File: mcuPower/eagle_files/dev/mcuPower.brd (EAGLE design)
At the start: 27 x 45.1 mm, 8 parts, among them P1 CR2032, P2 CR2032, U1 PQ070XF01SZH

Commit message: most complete to date files
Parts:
- moved P1 0.45 mm to (12.8, 32.5)
- moved P2 0.45 mm to (12.8, 32.5)
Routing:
- net GND: track 52.1 -> 50.4 mm
- net VCC: track 37.8 -> 38.6 mm
- net N$1: track 10.5 -> 11.0 mm
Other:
- board text added: "F. Lee mcuPower 8/25/13"
- board text removed: "F. Lee mcuPower 8/17/13"
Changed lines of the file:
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@@
 <layer number="27" name="tValues" color="7" fill="1" visible="yes" active="yes"/>
 <layer number="28" name="bValues" color="7" fill="1" visible="yes" active="yes"/>
-<layer number="29" name="tStop" color="7" fill="3" visible="yes" active="yes"/>
-<layer number="30" name="bStop" color="7" fill="6" visible="yes" active="yes"/>
-<layer number="31" name="tCream" color="7" fill="4" visible="yes" active="yes"/>
-<layer number="32" name="bCream" color="7" fill="5" visible="yes" active="yes"/>
+<layer number="29" name="tStop" color="7" fill="3" visible="no" active="yes"/>
+<layer number="30" name="bStop" color="7" fill="6" visible="no" active="yes"/>
+<layer number="31" name="tCream" color="7" fill="4" visible="no" active="yes"/>
+<layer number="32" name="bCream" color="7" fill="5" visible="no" active="yes"/>
 <layer number="33" name="tFinish" color="6" fill="3" visible="no" active="yes"/>
 <layer number="34" name="bFinish" color="6" fill="6" visible="no" active="yes"/>
@@
 <layer number="109" name="fp9" color="7" fill="1" visible="no" active="yes"/>
 <layer number="110" name="fp0" color="7" fill="1" visible="no" active="yes"/>
-<layer number="111" name="LPC17xx" color="7" fill="1" visible="yes" active="yes"/>
-<layer number="112" name="tSilk" color="7" fill="1" visible="yes" active="yes"/>
+<layer number="111" name="LPC17xx" color="7" fill="1" visible="no" active="yes"/>
+<layer number="112" name="tSilk" color="7" fill="1" visible="no" active="yes"/>
 <layer number="116" name="Patch_BOT" color="9" fill="4" visible="yes" active="yes"/>
-<layer number="121" name="_tsilk" color="7" fill="1" visible="yes" active="yes"/>
-<layer number="122" name="_bsilk" color="7" fill="1" visible="yes" active="yes"/>
-<layer number="123" name="tTestmark" color="7" fill="1" visible="yes" active="yes"/>
-<layer number="124" name="bTestmark" color="7" fill="1" visible="yes" active="yes"/>
-<layer number="125" name="_tNames" color="7" fill="1" visible="yes" active="yes"/>
-<layer number="126" name="_bNames" color="7" fill="1" visible="yes" active="yes"/>
-<layer number="127" name="_tValues" color="7" fill="1" visible="yes" active="yes"/>
-<layer number="128" name="_bValues" color="7" fill="1" visible="yes" active="yes"/>
-<layer number="131" name="tAdjust" color="7" fill="1" visible="yes" active="yes"/>
+<layer number="121" name="_tsilk" color="7" fill="1" visible="no" active="yes"/>
+<layer number="122" name="_bsilk" color="7" fill="1" visible="no" active="yes"/>
+<layer number="123" name="tTestmark" color="7" fill="1" visible="no" active="yes"/>
+<layer number="124" name="bTestmark" color="7" fill="1" visible="no" active="yes"/>
+<layer number="125" name="_tNames" color="7" fill="1" visible="no" active="yes"/>
+<layer number="126" name="_bNames" color="7" fill="1" visible="no" active="yes"/>
+<layer number="127" name="_tValues" color="7" fill="1" visible="no" active="yes"/>
+<layer number="128" name="_bValues" color="7" fill="1" visible="no" active="yes"/>
+<layer number="131" name="tAdjust" color="7" fill="1" visible="no" active="yes"/>
 <layer number="132" name="bAdjust" color="7" fill="1" visible="no" active="yes"/>
 <layer number="144" name="Drill_legend" color="7" fill="1" visible="yes" active="yes"/>
 <layer number="150" name="Notes" color="7" fill="1" visible="no" active="yes"/>
 <layer number="151" name="HeatSink" color="7" fill="1" visible="yes" active="yes"/>
-<layer number="152" name="_bDocu" color="7" fill="1" visible="yes" active="yes"/>
+<layer number="152" name="_bDocu" color="7" fill="1" visible="no" active="yes"/>
 <layer number="153" name="FabDoc1" color="6" fill="1" visible="no" active="no"/>
 <layer number="154" name="FabDoc2" color="2" fill="1" visible="no" active="no"/>
@@
 <wire x1="27.02" y1="45.09" x2="0.03" y2="45.05" width="0" layer="20"/>
 <wire x1="0.03" y1="45.05" x2="0" y2="0" width="0" layer="20"/>
-<text x="25" y="20.2" size="1.016" layer="16" rot="MR0">F. Lee
+<text x="25.3" y="20.5" size="1.016" layer="22" rot="MR0">F. Lee
 mcuPower
-8/17/13</text>
+8/25/13</text>
 </plain>
 <attributes>
@@
 <attribute name="NAME" x="3.78" y="21.08" size="1.27" layer="25" rot="R180"/>
 </element>
-<element name="P1" library="freddyLibr" package="CR2032/2025" value="CR2032" x="13" y="32.1" smashed="yes" rot="R90">
-<attribute name="NAME" x="4.71" y="26.44" size="1.27" layer="25" rot="R180"/>
-</element>
-<element name="P2" library="freddyLibr" package="CR2032/2025" value="CR2032" x="13" y="32.1" smashed="yes" rot="MR0">
-<attribute name="NAME" x="25.41" y="37.46" size="1.27" layer="26" rot="MR0"/>
+<element name="P1" library="freddyLibr" package="CR2032/2025" value="CR2032" x="12.8" y="32.5" smashed="yes" rot="R90">
+<attribute name="NAME" x="6.01" y="23.54" size="1.27" layer="25" rot="R180"/>
+</element>
+<element name="P2" library="freddyLibr" package="CR2032/2025" value="CR2032" x="12.8" y="32.5" smashed="yes" rot="MR0">
+<attribute name="NAME" x="21.01" y="41.16" size="1.27" layer="26" rot="MR0"/>
 </element>
 </elements>
@@
 <contactref element="C1" pad="1"/>
 <contactref element="U1" pad="VIN"/>
-<contactref element="P2" pad="VCC_2"/>
 <wire x1="22.4" y1="10.39" x2="11.82" y2="10.39" width="0.4064" layer="16"/>
 <wire x1="11.82" y1="10.39" x2="8.43" y2="7" width="0.4064" layer="16"/>
-<wire x1="23.4" y1="30.5" x2="23.4" y2="21.1" width="0.4064" layer="1"/>
-<wire x1="23.4" y1="21.1" x2="25.7" y2="18.8" width="0.4064" layer="1"/>
-<wire x1="25.7" y1="18.8" x2="25.7" y2="13.69" width="0.4064" layer="1"/>
-<wire x1="25.7" y1="13.69" x2="22.4" y2="10.39" width="0.4064" layer="1"/>
+<contactref element="P2" pad="VCC_2"/>
+<wire x1="23.2" y1="30.9" x2="23.2" y2="21" width="0.4064" layer="1"/>
+<wire x1="23.2" y1="21" x2="25.4" y2="18.8" width="0.4064" layer="1"/>
+<wire x1="25.4" y1="18.8" x2="25.4" y2="12.5" width="0.4064" layer="1"/>
+<wire x1="25.4" y1="12.5" x2="23.3" y2="10.4" width="0.4064" layer="1"/>
+<wire x1="23.3" y1="10.4" x2="22.41" y2="10.4" width="0.4064" layer="1"/>
+<wire x1="22.41" y1="10.4" x2="22.4" y2="10.39" width="0.4064" layer="1"/>
 </signal>
 <signal name="GND">
@@
 <contactref element="JP1" pad="1"/>
 <contactref element="U1" pad="GND"/>
-<contactref element="P1" pad="GND"/>
-<wire x1="13" y1="32.1" x2="13" y2="31.3" width="0.4064" layer="1"/>
-<wire x1="13" y1="31.3" x2="4.7" y2="23" width="0.4064" layer="1"/>
-<via x="4.7" y="23" extent="1-16" drill="0.6"/>
-<wire x1="4.7" y1="23" x2="4.74" y2="23" width="0.4064" layer="16"/>
-<wire x1="4.74" y1="23" x2="10.8" y2="16.94" width="0.4064" layer="16"/>
 <wire x1="10.8" y1="16.94" x2="10.8" y2="13.7" width="0.4064" layer="16"/>
 <wire x1="10.8" y1="13.7" x2="10.8" y2="12.28" width="0.4064" layer="16"/>
@@
 <wire x1="22.4" y1="15.47" x2="12.57" y2="15.47" width="0.4064" layer="16"/>
 <wire x1="12.57" y1="15.47" x2="10.8" y2="13.7" width="0.4064" layer="16"/>
+<contactref element="P1" pad="GND"/>
+<wire x1="10.8" y1="16.94" x2="10.8" y2="17" width="0.4064" layer="16"/>
+<wire x1="10.8" y1="17" x2="7.1" y2="20.7" width="0.4064" layer="16"/>
+<via x="7.1" y="20.7" extent="1-16" drill="0.6"/>
+<wire x1="7.1" y1="20.7" x2="7.1" y2="26.8" width="0.4064" layer="1"/>
+<wire x1="7.1" y1="26.8" x2="12.8" y2="32.5" width="0.4064" layer="1"/>
 </signal>
 <signal name="N$2">
@@
 <contactref element="JP1" pad="4"/>
 </signal>
+<signal name="N$3">
+</signal>
 <signal name="N$1">
 <contactref element="P1" pad="VCC_1"/>
 <contactref element="P2" pad="GND"/>
-<wire x1="11.5" y1="21.7" x2="12.8" y2="30.6" width="0.4064" layer="16"/>
-<wire x1="12.8" y1="30.6" x2="13" y2="32.1" width="0.4064" layer="16"/>
-</signal>
-<signal name="N$3">
+<wire x1="11.3" y1="22.1" x2="11.3" y2="31" width="0.4064" layer="16"/>
+<wire x1="11.3" y1="31" x2="12.8" y2="32.5" width="0.4064" layer="16"/>
 </signal>
 </signals>

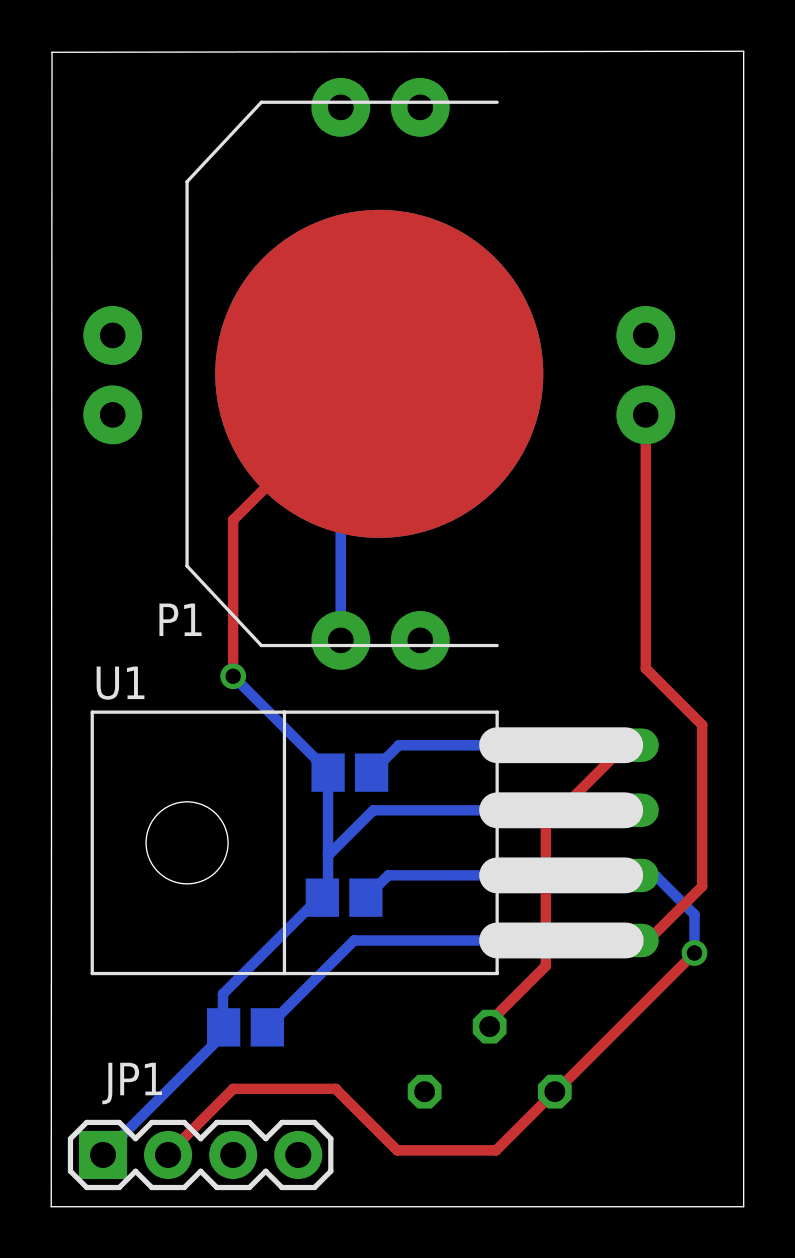
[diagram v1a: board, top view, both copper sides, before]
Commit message: additional tweaks to Eagle files. approaching final. focus here on ease of battery placement and space clearance.
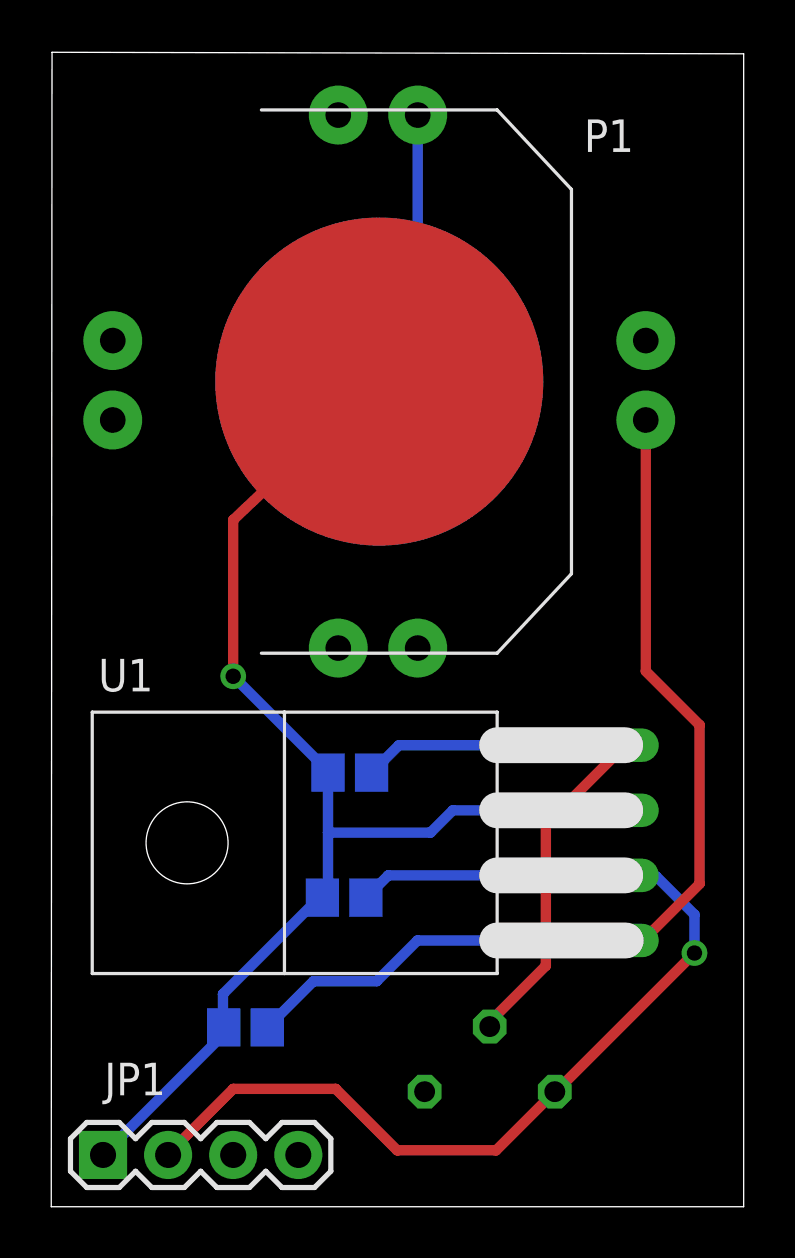
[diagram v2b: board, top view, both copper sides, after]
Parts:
- moved P1 0.30 mm to (12.8, 32.2), turned to 270 degrees
- moved P2 0.30 mm to (12.8, 32.2), turned to 180 degrees
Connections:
- net VCC: now also P2.VCC_3; no longer P2.VCC_2
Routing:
- net GND: track 50.4 -> 49.9 mm
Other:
- board size 27 x 45.1 mm -> 27 x 45 mm
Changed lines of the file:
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@@
 <plain>
 <wire x1="0" y1="0" x2="27.02" y2="0" width="0" layer="20"/>
-<wire x1="27.02" y1="0" x2="27.02" y2="45.09" width="0" layer="20"/>
-<wire x1="27.02" y1="45.09" x2="0.03" y2="45.05" width="0" layer="20"/>
+<wire x1="27.02" y1="0" x2="27.02" y2="44.99" width="0" layer="20"/>
+<wire x1="27.02" y1="44.99" x2="0.03" y2="45.05" width="0" layer="20"/>
 <wire x1="0.03" y1="45.05" x2="0" y2="0" width="0" layer="20"/>
-<text x="25.3" y="20.5" size="1.016" layer="22" rot="MR0">F. Lee
+<text x="25.1" y="20.2" size="1.016" layer="22" rot="MR0">F. Lee
 mcuPower
 8/25/13</text>
@@
 </element>
 <element name="C1" library="resistor" package="C0805" value="" x="7.58" y="7" smashed="yes" rot="MR0">
-<attribute name="NAME" x="11.969" y="6.416" size="1.27" layer="26" rot="MR0"/>
+<attribute name="NAME" x="12.369" y="5.816" size="1.27" layer="26" rot="MR0"/>
 <attribute name="VALUE" x="8.469" y="4.714" size="1.27" layer="28" rot="MR0"/>
 </element>
@@
 </element>
 <element name="U1" library="freddyLibr" package="TO220-4" value="PQ070XF01SZH" x="9.1" y="14.2" smashed="yes" rot="R90">
-<attribute name="NAME" x="3.78" y="21.08" size="1.27" layer="25" rot="R180"/>
-</element>
-<element name="P1" library="freddyLibr" package="CR2032/2025" value="CR2032" x="12.8" y="32.5" smashed="yes" rot="R90">
-<attribute name="NAME" x="6.01" y="23.54" size="1.27" layer="25" rot="R180"/>
-</element>
-<element name="P2" library="freddyLibr" package="CR2032/2025" value="CR2032" x="12.8" y="32.5" smashed="yes" rot="MR0">
-<attribute name="NAME" x="21.01" y="41.16" size="1.27" layer="26" rot="MR0"/>
+<attribute name="NAME" x="3.98" y="21.38" size="1.27" layer="25" rot="R180"/>
+</element>
+<element name="P1" library="freddyLibr" package="CR2032/2025" value="CR2032" x="12.8" y="32.2" smashed="yes" rot="R270">
+<attribute name="NAME" x="20.79" y="41.16" size="1.27" layer="25"/>
+</element>
+<element name="P2" library="freddyLibr" package="CR2032/2025" value="CR2032" x="12.8" y="32.2" smashed="yes" rot="MR180">
+<attribute name="NAME" x="21.29" y="39.84" size="1.27" layer="26" rot="MR180"/>
 </element>
 </elements>
@@
 <contactref element="C1" pad="1"/>
 <contactref element="U1" pad="VIN"/>
-<wire x1="22.4" y1="10.39" x2="11.82" y2="10.39" width="0.4064" layer="16"/>
-<wire x1="11.82" y1="10.39" x2="8.43" y2="7" width="0.4064" layer="16"/>
-<contactref element="P2" pad="VCC_2"/>
-<wire x1="23.2" y1="30.9" x2="23.2" y2="21" width="0.4064" layer="1"/>
-<wire x1="23.2" y1="21" x2="25.4" y2="18.8" width="0.4064" layer="1"/>
-<wire x1="25.4" y1="18.8" x2="25.4" y2="12.5" width="0.4064" layer="1"/>
-<wire x1="25.4" y1="12.5" x2="23.3" y2="10.4" width="0.4064" layer="1"/>
-<wire x1="23.3" y1="10.4" x2="22.41" y2="10.4" width="0.4064" layer="1"/>
+<contactref element="P2" pad="VCC_3"/>
+<wire x1="23.2" y1="30.7" x2="23.2" y2="20.9" width="0.4064" layer="1"/>
+<wire x1="23.2" y1="20.9" x2="25.3" y2="18.8" width="0.4064" layer="1"/>
+<wire x1="25.3" y1="18.8" x2="25.3" y2="12.6" width="0.4064" layer="1"/>
+<wire x1="25.3" y1="12.6" x2="23.1" y2="10.4" width="0.4064" layer="1"/>
+<wire x1="23.1" y1="10.4" x2="22.41" y2="10.4" width="0.4064" layer="1"/>
 <wire x1="22.41" y1="10.4" x2="22.4" y2="10.39" width="0.4064" layer="1"/>
+<wire x1="22.4" y1="10.39" x2="14.29" y2="10.39" width="0.4064" layer="16"/>
+<wire x1="14.29" y1="10.39" x2="12.7" y2="8.8" width="0.4064" layer="16"/>
+<wire x1="12.7" y1="8.8" x2="10.23" y2="8.8" width="0.4064" layer="16"/>
+<wire x1="10.23" y1="8.8" x2="8.43" y2="7" width="0.4064" layer="16"/>
 </signal>
 <signal name="GND">
@@
 <contactref element="JP1" pad="1"/>
 <contactref element="U1" pad="GND"/>
-<wire x1="10.8" y1="16.94" x2="10.8" y2="13.7" width="0.4064" layer="16"/>
-<wire x1="10.8" y1="13.7" x2="10.8" y2="12.28" width="0.4064" layer="16"/>
-<wire x1="10.8" y1="12.28" x2="10.58" y2="12.06" width="0.4064" layer="16"/>
 <wire x1="10.58" y1="12.06" x2="10.46" y2="12.06" width="0.4064" layer="16"/>
 <wire x1="10.46" y1="12.06" x2="6.7" y2="8.3" width="0.4064" layer="16"/>
@@
 <wire x1="6.73" y1="7" x2="6.73" y2="6.73" width="0.4064" layer="16"/>
 <wire x1="6.73" y1="6.73" x2="2.02" y2="2.02" width="0.4064" layer="16"/>
-<wire x1="22.4" y1="15.47" x2="12.57" y2="15.47" width="0.4064" layer="16"/>
-<wire x1="12.57" y1="15.47" x2="10.8" y2="13.7" width="0.4064" layer="16"/>
 <contactref element="P1" pad="GND"/>
 <wire x1="10.8" y1="16.94" x2="10.8" y2="17" width="0.4064" layer="16"/>
@@
 <via x="7.1" y="20.7" extent="1-16" drill="0.6"/>
 <wire x1="7.1" y1="20.7" x2="7.1" y2="26.8" width="0.4064" layer="1"/>
-<wire x1="7.1" y1="26.8" x2="12.8" y2="32.5" width="0.4064" layer="1"/>
+<wire x1="7.1" y1="26.8" x2="12.8" y2="32.2" width="0.4064" layer="1"/>
+<wire x1="10.8" y1="16.94" x2="10.8" y2="14.6" width="0.4064" layer="16"/>
+<wire x1="10.8" y1="14.6" x2="10.8" y2="12.28" width="0.4064" layer="16"/>
+<wire x1="10.8" y1="12.28" x2="10.58" y2="12.06" width="0.4064" layer="16"/>
+<wire x1="22.4" y1="15.47" x2="15.67" y2="15.47" width="0.4064" layer="16"/>
+<wire x1="15.67" y1="15.47" x2="14.8" y2="14.6" width="0.4064" layer="16"/>
+<wire x1="14.8" y1="14.6" x2="10.8" y2="14.6" width="0.4064" layer="16"/>
 </signal>
 <signal name="N$2">
@@
 <contactref element="P1" pad="VCC_1"/>
 <contactref element="P2" pad="GND"/>
-<wire x1="11.3" y1="22.1" x2="11.3" y2="31" width="0.4064" layer="16"/>
-<wire x1="11.3" y1="31" x2="12.8" y2="32.5" width="0.4064" layer="16"/>
+<wire x1="14.3" y1="42.6" x2="14.3" y2="34" width="0.4064" layer="16"/>
+<wire x1="14.3" y1="34" x2="12.8" y2="32.2" width="0.4064" layer="16"/>
 </signal>
 </signals>
